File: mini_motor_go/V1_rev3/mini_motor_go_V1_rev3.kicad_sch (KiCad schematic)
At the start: 30 parts, among them J10 Conn_01x02_Pin, J11 USB4520-03-0-A_REVA, J12 BM05B-SRSS-TB_LF__SN_, J13 BM05B-SRSS-TB_LF__SN_, J3 I2C_STANDARDQWIIC, J5 I2C_STANDARDQWIIC, J9 Conn_01x09_Pin, U1 ESP32-S3-WROOM-1

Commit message: updated part numbers for final review, compared eschema footprints to pcb file. see notes in eschema part list. TS
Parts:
- D1: note consider select different colors for each -> red - footprint match
- D2: LCSC Part Number C965812 -> C965814; Manufacturer_Part_Number XL-2012SURC -> XL-2012UYC; note consider select different colors for each -> yellow - footprint match
- D3: LCSC Part Number C965812 -> C965815; Manufacturer_Part_Number XL-2012SURC -> XL-2012UGC; note consider select different colors for each -> green - footprint match
- J10: LCSC Part Number (none) -> DNP; Manufacturer_Name (none) -> DNP; Manufacturer_Part_Number (none) -> DNP; note this one is odd, but we are combining j9 and j10 into one 1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 -> DNP
- J11: LCSC Part Number n/a -> C2965608; Manufacturer_Name GCT -> SHOU HAN; Manufacturer_Part_Number USB4520-03-0-A -> TYPE-C16P3MDDGP073; note from last order we used: C2965608 -> footprint match
- J12, J13, R20, R21, R22, R23, R24, R25, R26, R27, R28, R29, R30, R31, R32, R33: note (none) -> footprint match
- J3, J5, U1: note (none) -> footprint discrepancy
- J6, J7: LCSC Part Number C2800385 -> C2689521; Manufacturer_Part_Number PTS526 SM08 SMTR2 LFS -> PTS526SK15SMTR2LFS; note use button part sent in engineering channel -> footprint match
- J9: LCSC Part Number C6332202 -> DNP; Manufacturer_Name Hanbo Electronic -> DNP; Manufacturer_Part_Number HB-PH3-25419PB2GOP -> DNP; note this one is odd, but we are combining j9 and j10 into one 1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 -> DNP
- JP1, JP2, JP3: LCSC Part Number (none) -> DNP; Manufacturer_Name (none) -> DNP; Manufacturer_Part_Number (none) -> DNP

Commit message: added gerber, centroid, and bom exports for quotes
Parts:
- D1, D2, D3, J11, J12, J13, J3, J5, J6, J7, R20, R21, R22, R23, R24, R25, R26, R27, R28, R29, R30, R31, R32, R33, U1: Customer Supply (none) -> N
- J10, J9, JP1, JP2, JP3: Customer Supply (none) -> DNP
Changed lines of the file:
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@@
+      (effects (font (size 1.27 1.27)) hide)
+    )
+    (property "Customer Supply" "N" (at 101.6 146.05 0)
       (effects (font (size 1.27 1.27)) hide)
     )
@@
       (effects (font (size 1.27 1.27)) hide)
     )
+    (property "Customer Supply" "N" (at 203.2 95.25 0)
+      (effects (font (size 1.27 1.27)) hide)
+    )
     (pin "1")
     (pin "2")
@@
       (effects (font (size 1.27 1.27)) hide)
     )
+    (property "Customer Supply" "N" (at 205.74 38.1 0)
+      (effects (font (size 1.27 1.27)) hide)
+    )
     (pin "1")
     (pin "2")
@@
     )
     (property "Manufacturer_Part_Number" "CR0402FF5101G" (at 40.64 74.93 0)
+      (effects (font (size 1.27 1.27)) hide)
+    )
+    (property "Customer Supply" "N" (at 40.64 74.93 0)
       (effects (font (size 1.27 1.27)) hide)
     )
@@
     )
     (property "Manufacturer_Part_Number" "TYPE-C16P3MDDGP073" (at 71.12 157.48 0)
+      (effects (font (size 1.27 1.27)) hide)
+    )
+    (property "Customer Supply" "N" (at 71.12 157.48 0)
       (effects (font (size 1.27 1.27)) hide)
     )
@@
       (effects (font (size 1.27 1.27)) hide)
     )
+    (property "Customer Supply" "N" (at 19.05 185.42 0)
+      (effects (font (size 1.27 1.27)) hide)
+    )
     (pin "1")
     (pin "2")
@@
     )
     (property "Manufacturer_Part_Number" "ESP32-S3-WROOM-1-N8" (at 95.25 66.04 0)
+      (effects (font (size 1.27 1.27)) hide)
+    )
+    (property "Customer Supply" "N" (at 95.25 66.04 0)
       (effects (font (size 1.27 1.27)) hide)
     )
@@
       (effects (font (size 1.27 1.27)) hide)
     )
+    (property "Customer Supply" "N" (at 144.78 152.4 0)
+      (effects (font (size 1.27 1.27)) hide)
+    )
     (pin "1")
     (pin "2")
@@
       (effects (font (size 1.27 1.27)) hide)
     )
+    (property "Customer Supply" "N" (at 27.94 129.54 0)
+      (effects (font (size 1.27 1.27)) hide)
+    )
     (pin "1")
     (pin "2")
@@
     )
     (property "Manufacturer_Part_Number" "SM04B-SRSS-TB(LF)(SN)" (at 41.91 129.54 0)
+      (effects (font (size 1.27 1.27)) hide)
+    )
+    (property "Customer Supply" "N" (at 41.91 129.54 0)
       (effects (font (size 1.27 1.27)) hide)
     )
@@
       (effects (font (size 1.27 1.27)) hide)
     )
+    (property "Customer Supply" "N" (at 27.305 104.775 0)
+      (effects (font (size 1.27 1.27)) hide)
+    )
     (pin "1")
     (pin "2")
@@
       (effects (font (size 1.27 1.27)) hide)
     )
+    (property "Customer Supply" "N" (at 38.1 185.42 0)
+      (effects (font (size 1.27 1.27)) hide)
+    )
     (pin "1")
     (pin "2")
@@
       (effects (font (size 1.27 1.27)) hide)
     )
+    (property "Customer Supply" "N" (at 38.1 176.53 0)
+      (effects (font (size 1.27 1.27)) hide)
+    )
     (pin "1")
     (pin "2")
@@
     )
     (property "note" "red - footprint match " (at 19.05 176.53 0)
+      (effects (font (size 1.27 1.27)) hide)
+    )
+    (property "Customer Supply" "N" (at 19.05 176.53 0)
       (effects (font (size 1.27 1.27)) hide)
     )
@@
       (effects (font (size 1.27 1.27)) hide)
     )
+    (property "Customer Supply" "N" (at 161.29 126.365 0)
+      (effects (font (size 1.27 1.27)) hide)
+    )
     (pin "1")
     (pin "2")
@@
       (effects (font (size 1.27 1.27)) hide)
     )
+    (property "Customer Supply" "N" (at 163.83 126.365 0)
+      (effects (font (size 1.27 1.27)) hide)
+    )
     (pin "1")
     (pin "2")
@@
     )
     (property "note" "yellow - footprint match " (at 27.94 176.53 0)
+      (effects (font (size 1.27 1.27)) hide)
+    )
+    (property "Customer Supply" "N" (at 27.94 176.53 0)
       (effects (font (size 1.27 1.27)) hide)
     )
@@
       (effects (font (size 1.27 1.27)) hide)
     )
+    (property "Customer Supply" "N" (at 213.36 48.26 0)
+      (effects (font (size 1.27 1.27)) hide)
+    )
     (pin "1")
     (pin "2")
@@
       (effects (font (size 1.27 1.27)) hide)
     )
+    (property "Customer Supply" "DNP" (at 156.21 30.48 0)
+      (effects (font (size 1.27 1.27)) hide)
+    )
     (pin "1")
     (pin "2")
@@
     )
     (property "Manufacturer_Part_Number" "DNP" (at 38.1 168.91 0)
+      (effects (font (size 1.27 1.27)) hide)
+    )
+    (property "Customer Supply" "DNP" (at 38.1 168.91 0)
       (effects (font (size 1.27 1.27)) hide)
     )
@@
     )
     (property "Manufacturer_Part_Number" "DNP" (at 22.86 43.18 0)
+      (effects (font (size 1.27 1.27)) hide)
+    )
+    (property "Customer Supply" "DNP" (at 22.86 43.18 0)
       (effects (font (size 1.27 1.27)) hide)
     )
@@
       (effects (font (size 1.27 1.27)) hide)
     )
+    (property "Customer Supply" "DNP" (at 19.05 168.91 0)
+      (effects (font (size 1.27 1.27)) hide)
+    )
     (pin "1")
     (pin "2")
@@
       (effects (font (size 1.27 1.27)) hide)
     )
+    (property "Customer Supply" "DNP" (at 27.94 168.91 0)
+      (effects (font (size 1.27 1.27)) hide)
+    )
     (pin "1")
     (pin "2")
@@
       (effects (font (size 1.27 1.27)) hide)
     )
+    (property "Customer Supply" "N" (at 101.6 142.24 0)
+      (effects (font (size 1.27 1.27)) hide)
+    )
     (pin "1")
     (pin "2")
@@
     )
     (property "Manufacturer_Part_Number" "SM05B-NSHSS-TB(LF)(SN)" (at 175.26 152.4 0)
+      (effects (font (size 1.27 1.27)) hide)
+    )
+    (property "Customer Supply" "N" (at 175.26 152.4 0)
       (effects (font (size 1.27 1.27)) hide)
     )
@@
       (effects (font (size 1.27 1.27)) hide)
     )
+    (property "Customer Supply" "N" (at 24.765 104.775 0)
+      (effects (font (size 1.27 1.27)) hide)
+    )
     (pin "1")
     (pin "2")
@@
       (effects (font (size 1.27 1.27)) hide)
     )
+    (property "Customer Supply" "N" (at 25.4 81.28 0)
+      (effects (font (size 1.27 1.27)) hide)
+    )
     (pin "1")
     (pin "2")
@@
       (effects (font (size 1.27 1.27)) hide)
     )
+    (property "Customer Supply" "N" (at 102.87 156.21 0)
+      (effects (font (size 1.27 1.27)) hide)
+    )
     (pin "1")
     (pin "2")
@@
       (effects (font (size 1.27 1.27)) hide)
     )
+    (property "Customer Supply" "N" (at 27.94 185.42 0)
+      (effects (font (size 1.27 1.27)) hide)
+    )
     (pin "1")
     (pin "2")
@@
       (effects (font (size 1.27 1.27)) hide)
     )
+    (property "Customer Supply" "N" (at 102.87 151.13 0)
+      (effects (font (size 1.27 1.27)) hide)
+    )

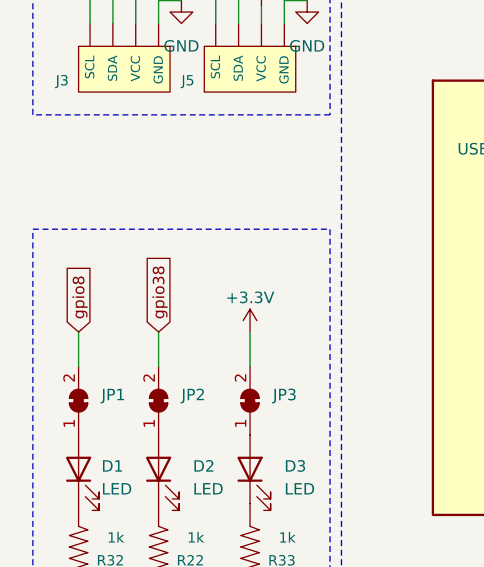
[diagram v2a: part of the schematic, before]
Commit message: fix indicator led silkscreen io8 to io47
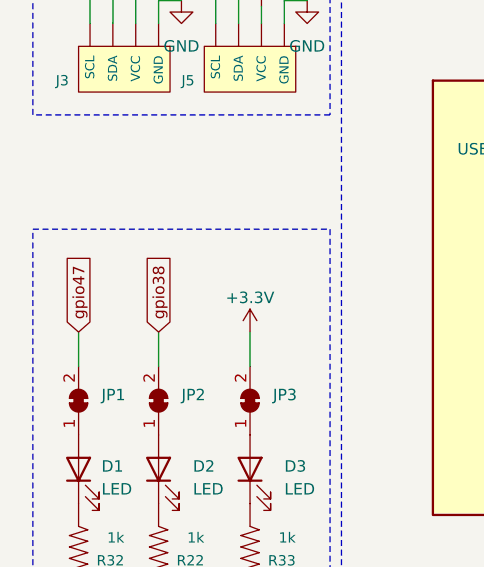
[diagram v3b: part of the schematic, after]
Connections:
- net gpio8 is gone; now on net gpio47: JP1.2 (B)
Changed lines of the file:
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@@
-    )
-  )
-  (global_label "gpio8" (shape input) (at 19.05 161.29 90) (fields_autoplaced)
-    (effects (font (size 1.27 1.27)) (justify left))
-    (property "Intersheetrefs" "${INTERSHEET_REFS}" (at 19.05 153.1229 90)
-      (effects (font (size 1.27 1.27)) (justify left) hide)
     )
   )
@@
       (effects (font (size 1.27 1.27)) (justify left) hide)
     )
+  )
+  (global_label "gpio47" (shape input) (at 19.05 161.29 90) (fields_autoplaced)
+    (effects (font (size 1.27 1.27)) (justify left))
+    (property "Intersheetrefs" "${INTERSHEET_REFS}" (at 19.05 151.9134 90)
+      (effects (font (size 1.27 1.27)) (justify left) hide)
+    )
